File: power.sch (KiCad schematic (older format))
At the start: 17 parts, among them J4 BATTERY, U1 OpAmp-TLV2374, U10 REG-7805, U2 Comp-LM339, U3 4000series-4094, U4 4000series-4024, U5 4000series-4051, U6 4000series-4051, U7 555_BJH

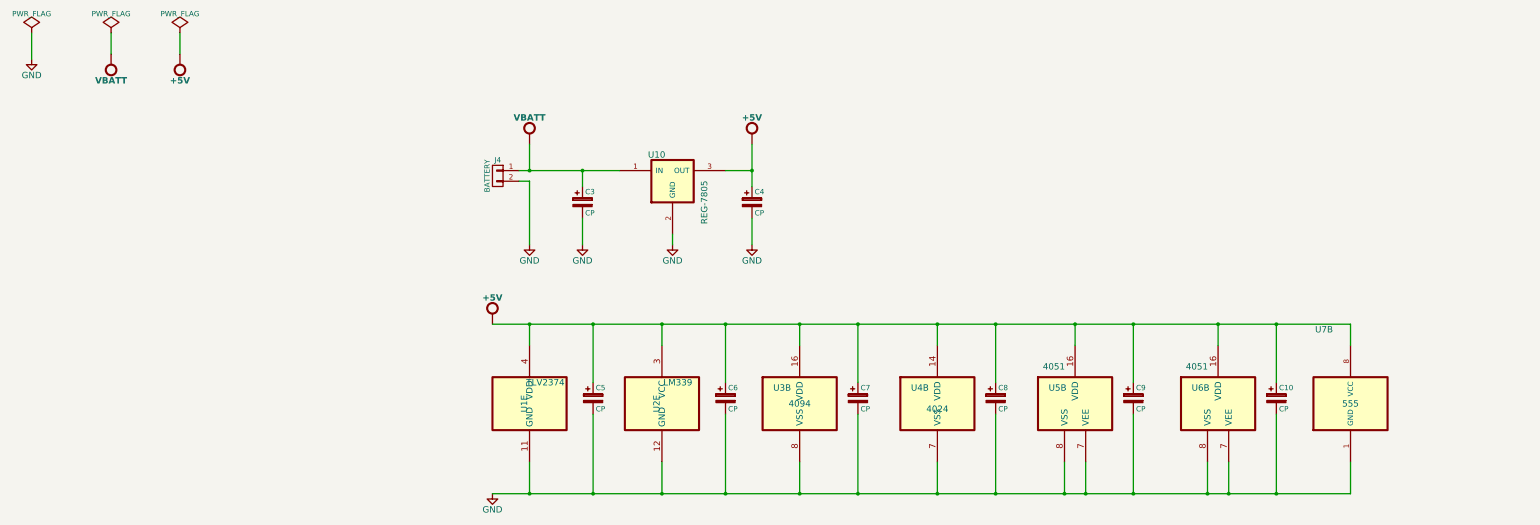
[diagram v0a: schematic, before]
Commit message: Added battery low detector and stripboard design (VeeCad)
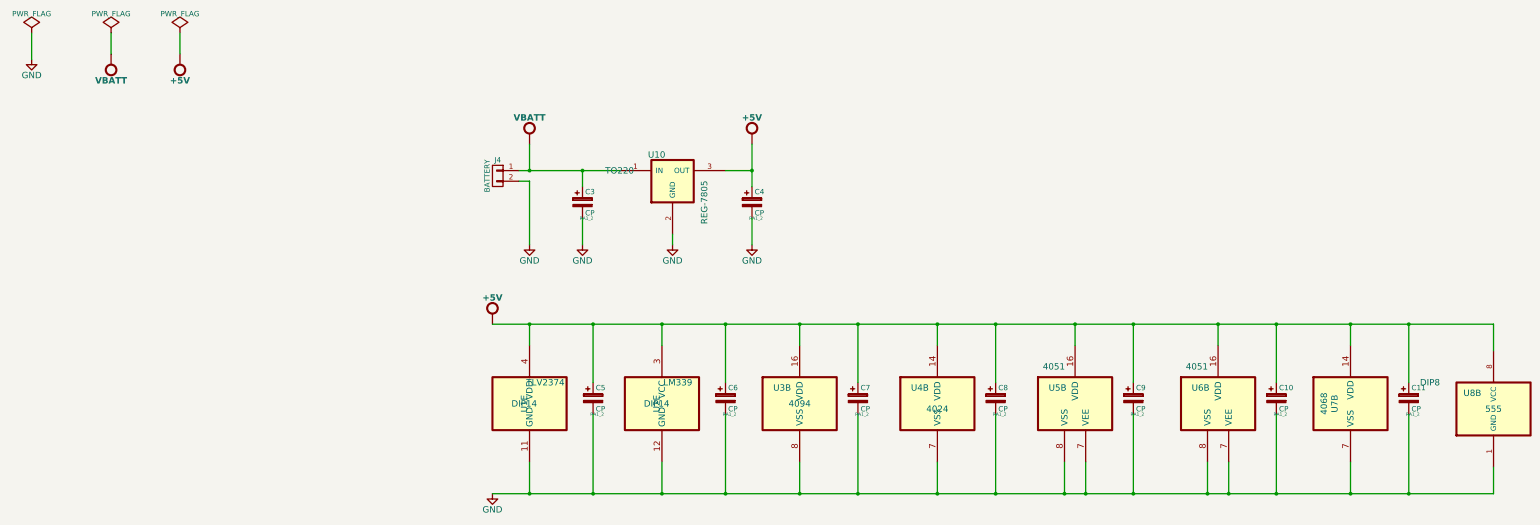
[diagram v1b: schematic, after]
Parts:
- added C11: CP, RA1_2, symbol CP
- added U7: 4000series-4068, DIP14, symbol 4000series-4068
- C10, C3, C4, C5, C6, C7, C8, C9: footprint (none) -> RA1_2
- J4: footprint (none) -> SIP2
- U1, U2: footprint (none) -> DIP14
- U10: footprint (none) -> TO220
- U8: renamed from U7; footprint (none) -> DIP8
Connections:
- net +5V: now also C11.1, U7.14 (VDD)
- net GND: now also C11.2, U7.7 (VSS)
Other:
- moved on the sheet: U8B

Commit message: Separated .net files for VeeCAD and KiCAD.  Associated footprints for KiCAD and started board layout
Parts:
- C10, C11, C3, C4, C5, C6, C7, C8, C9: footprint RA1_2 -> Capacitors_ThroughHole:C_Radial_D5_L6_P2.5
- J4: footprint SIP2 -> connector-bjh:HEAD-1row-2.54mm-2way
- U1, U2, U4, U7: footprint DIP14 -> Sockets_DIP:DIP-14__300_ELL
- U10: footprint TO220 -> Transistors_TO-220:TO-220_Neutral123_Vertical
- U3, U5, U6: footprint DIP16 -> Sockets_DIP:DIP-16__300_ELL
- U8: footprint DIP8 -> Sockets_DIP:DIP-8__300_ELL
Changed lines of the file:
@@
 $Descr A4 11693 8268
 encoding utf-8
-Sheet 2 4
+Sheet 2 3
 Title ""
 Date ""
@@
 F 0 "U10" H 2400 1300 60  0000 C CNN
 F 1 "REG-7805" V 2850 850 60  0000 C CNN
-F 2 "TO220" H 2050 1150 60  0000 C CNN
+F 2 "Transistors_TO-220:TO-220_Neutral123_Vertical" H 2050 1150 60  0000 C CNN
 F 3 "" H 2050 1150 60  0000 C CNN
 	1    2050 1150
@@
 F 0 "C3" H 1725 1550 50  0000 L CNN
 F 1 "CP" H 1725 1350 50  0000 L CNN
-F 2 "RA1_2" H 1738 1300 30  0000 C CNN
+F 2 "Capacitors_ThroughHole:C_Radial_D5_L6_P2.5" H 1738 1300 30  0000 C CNN
 F 3 "" H 1700 1450 60  0000 C CNN
 	1    1700 1450
@@
 F 0 "C4" H 3325 1550 50  0000 L CNN
 F 1 "CP" H 3325 1350 50  0000 L CNN
-F 2 "RA1_2" H 3338 1300 30  0000 C CNN
+F 2 "Capacitors_ThroughHole:C_Radial_D5_L6_P2.5" H 3338 1300 30  0000 C CNN
 F 3 "" H 3300 1450 60  0000 C CNN
 	1    3300 1450
@@
 F 0 "U1" V 1150 3350 60  0000 C CNN
 F 1 "OpAmp-TLV2374" H 1200 3650 60  0001 C CNN
-F 2 "DIP14" H 1150 3350 60  0000 C CNN
+F 2 "Sockets_DIP:DIP-14__300_ELL" H 1150 3350 60  0000 C CNN
 F 3 "" H 1150 3350 60  0000 C CNN
 F 4 "TLV2374" H 1350 3550 60  0000 C CNN "Device"
@@
 F 0 "U2" V 2400 3350 60  0000 C CNN
 F 1 "Comp-LM339" H 2450 3650 60  0001 C CNN
-F 2 "DIP14" H 2400 3350 60  0000 C CNN
+F 2 "Sockets_DIP:DIP-14__300_ELL" H 2400 3350 60  0000 C CNN
 F 3 "" H 2400 3350 60  0000 C CNN
 F 4 "LM339" H 2600 3550 60  0000 C CNN "Device"
@@
 F 0 "U3" H 3500 3500 60  0000 L CNN
 F 1 "4000series-4094" H 3400 3950 60  0001 L CNN
-F 2 "DIP16" H 3750 3300 60  0001 C CNN
+F 2 "Sockets_DIP:DIP-16__300_ELL" H 3750 3300 60  0001 C CNN
 F 3 "" H 3950 3300 60  0000 C CNN
 F 4 "4094" H 3750 3350 60  0000 C CNN "Device"
@@
 F 0 "U4" H 4800 3500 60  0000 L CNN
 F 1 "4000series-4024" H 4700 3950 60  0001 L CNN
-F 2 "DIP14" H 5050 3300 60  0001 C CNN
+F 2 "Sockets_DIP:DIP-14__300_ELL" H 5050 3300 60  0001 C CNN
 F 3 "" H 5250 3300 60  0000 C CNN
 F 4 "4024" H 5050 3300 60  0000 C CNN "Device"
@@
 F 0 "U5" H 6100 3500 60  0000 L CNN
 F 1 "4000series-4051" H 6000 3950 60  0001 L CNN
-F 2 "DIP16" H 6350 3300 60  0001 C CNN
+F 2 "Sockets_DIP:DIP-16__300_ELL" H 6350 3300 60  0001 C CNN
 F 3 "" H 6550 3300 60  0000 C CNN
 F 4 "4051" H 6150 3700 60  0000 C CNN "Device"
@@
 F 0 "U6" H 7450 3500 60  0000 L CNN
 F 1 "4000series-4051" H 7350 3950 60  0001 L CNN
-F 2 "DIP16" H 7700 3300 60  0001 C CNN
+F 2 "Sockets_DIP:DIP-16__300_ELL" H 7700 3300 60  0001 C CNN
 F 3 "" H 7900 3300 60  0000 C CNN
 F 4 "4051" H 7500 3700 60  0000 C CNN "Device"
@@
 F 0 "U8" H 10100 3550 60  0000 C CNN
 F 1 "555_BJH" V 10750 2950 60  0001 C CNN
-F 2 "DIP8" H 9700 3650 60  0000 C CNN
+F 2 "Sockets_DIP:DIP-8__300_ELL" H 9700 3650 60  0000 C CNN
 F 3 "" H 9700 3650 60  0000 C CNN
 F 4 "555" H 10300 3400 60  0000 C CNN "Device"
@@
 F 0 "C5" H 1825 3400 50  0000 L CNN
 F 1 "CP" H 1825 3200 50  0000 L CNN
-F 2 "RA1_2" H 1838 3150 30  0000 C CNN
+F 2 "Capacitors_ThroughHole:C_Radial_D5_L6_P2.5" H 1838 3150 30  0000 C CNN
 F 3 "" H 1800 3300 60  0000 C CNN
 	1    1800 3300
@@
 F 0 "C6" H 3075 3400 50  0000 L CNN
 F 1 "CP" H 3075 3200 50  0000 L CNN
-F 2 "RA1_2" H 3088 3150 30  0000 C CNN
+F 2 "Capacitors_ThroughHole:C_Radial_D5_L6_P2.5" H 3088 3150 30  0000 C CNN
 F 3 "" H 3050 3300 60  0000 C CNN
 	1    3050 3300
@@
 F 0 "C7" H 4325 3400 50  0000 L CNN
 F 1 "CP" H 4325 3200 50  0000 L CNN
-F 2 "RA1_2" H 4338 3150 30  0000 C CNN
+F 2 "Capacitors_ThroughHole:C_Radial_D5_L6_P2.5" H 4338 3150 30  0000 C CNN
 F 3 "" H 4300 3300 60  0000 C CNN
 	1    4300 3300
@@
 F 0 "C8" H 5625 3400 50  0000 L CNN
 F 1 "CP" H 5625 3200 50  0000 L CNN
-F 2 "RA1_2" H 5638 3150 30  0000 C CNN
+F 2 "Capacitors_ThroughHole:C_Radial_D5_L6_P2.5" H 5638 3150 30  0000 C CNN
 F 3 "" H 5600 3300 60  0000 C CNN
 	1    5600 3300
@@
 F 0 "C9" H 6925 3400 50  0000 L CNN
 F 1 "CP" H 6925 3200 50  0000 L CNN
-F 2 "RA1_2" H 6938 3150 30  0000 C CNN
+F 2 "Capacitors_ThroughHole:C_Radial_D5_L6_P2.5" H 6938 3150 30  0000 C CNN
 F 3 "" H 6900 3300 60  0000 C CNN
 	1    6900 3300
@@
 F 0 "C10" H 8275 3400 50  0000 L CNN
 F 1 "CP" H 8275 3200 50  0000 L CNN
-F 2 "RA1_2" H 8288 3150 30  0000 C CNN
+F 2 "Capacitors_ThroughHole:C_Radial_D5_L6_P2.5" H 8288 3150 30  0000 C CNN
 F 3 "" H 8250 3300 60  0000 C CNN
 	1    8250 3300
@@
 F 0 "U7" V 8800 3350 60  0000 C CNN
 F 1 "4000series-4068" H 8950 3650 60  0001 C CNN
-F 2 "DIP14" H 8900 3350 60  0001 C CNN
+F 2 "Sockets_DIP:DIP-14__300_ELL" H 8900 3350 60  0001 C CNN
 F 3 "" H 8900 3350 60  0000 C CNN
 F 4 "4068" V 8700 3350 60  0000 C CNN "Device"
@@
 F 0 "C11" H 9525 3400 50  0000 L CNN
 F 1 "CP" H 9525 3200 50  0000 L CNN
-F 2 "RA1_2" H 9538 3150 30  0000 C CNN
+F 2 "Capacitors_ThroughHole:C_Radial_D5_L6_P2.5" H 9538 3150 30  0000 C CNN
 F 3 "" H 9500 3300 60  0000 C CNN
 	1    9500 3300
@@
 F 0 "J4" H 900 1350 50  0000 C CNN
 F 1 "BATTERY" V 1000 1200 50  0000 C CNN
-F 2 "SIP2" H 900 1200 60  0001 C CNN
+F 2 "connector-bjh:HEAD-1row-2.54mm-2way" H 900 1200 60  0001 C CNN
 F 3 "" H 900 1200 60  0000 C CNN
 	1    900  1200
